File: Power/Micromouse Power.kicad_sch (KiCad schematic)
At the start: 24 parts, among them J1 Conn_02x08_Odd_Even, SW1 SW_SPST, U1 TP4056, U2 L9110S, U3 L9110S

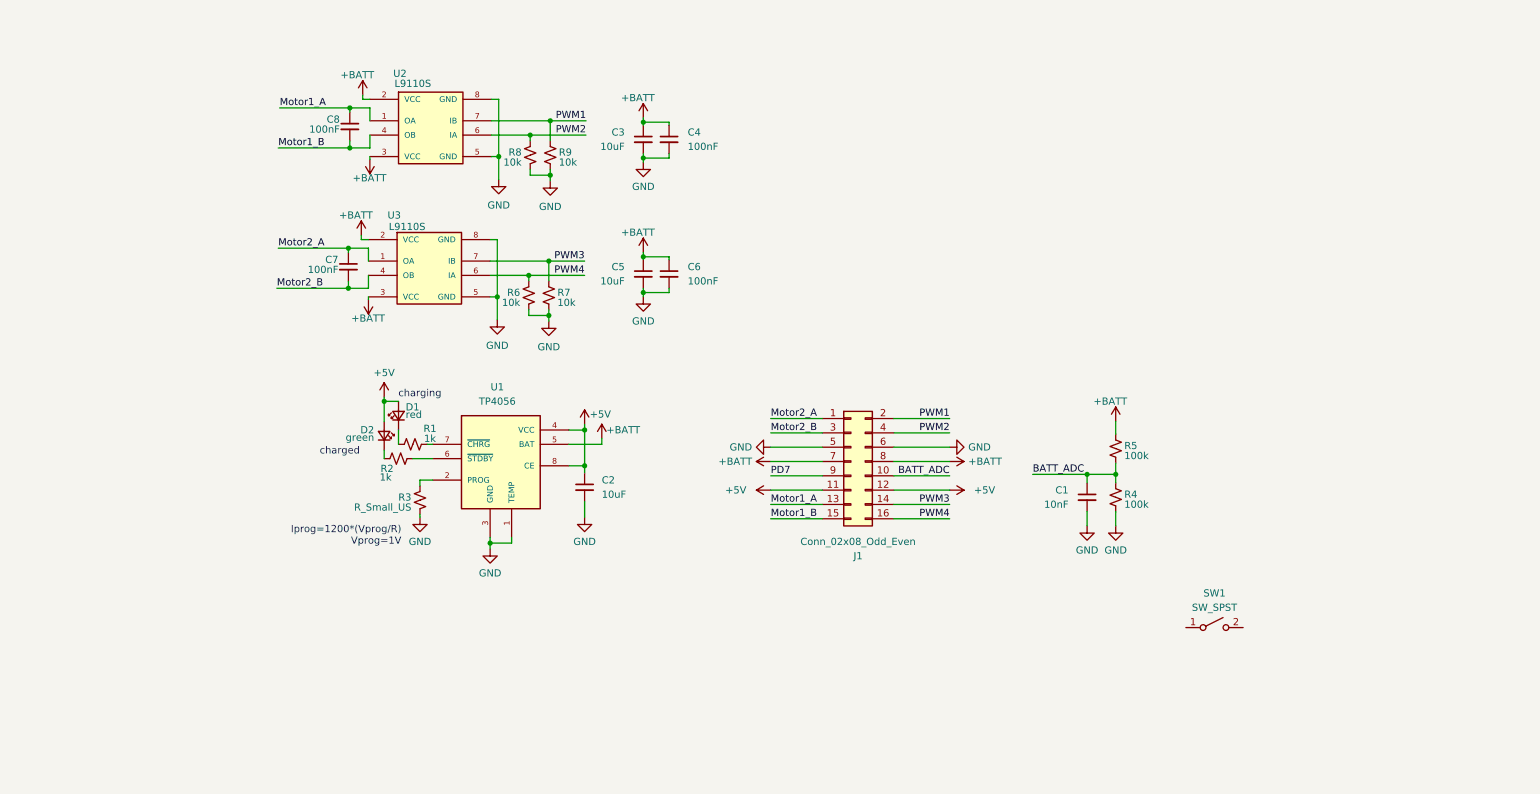
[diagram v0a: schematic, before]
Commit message: Added power flags
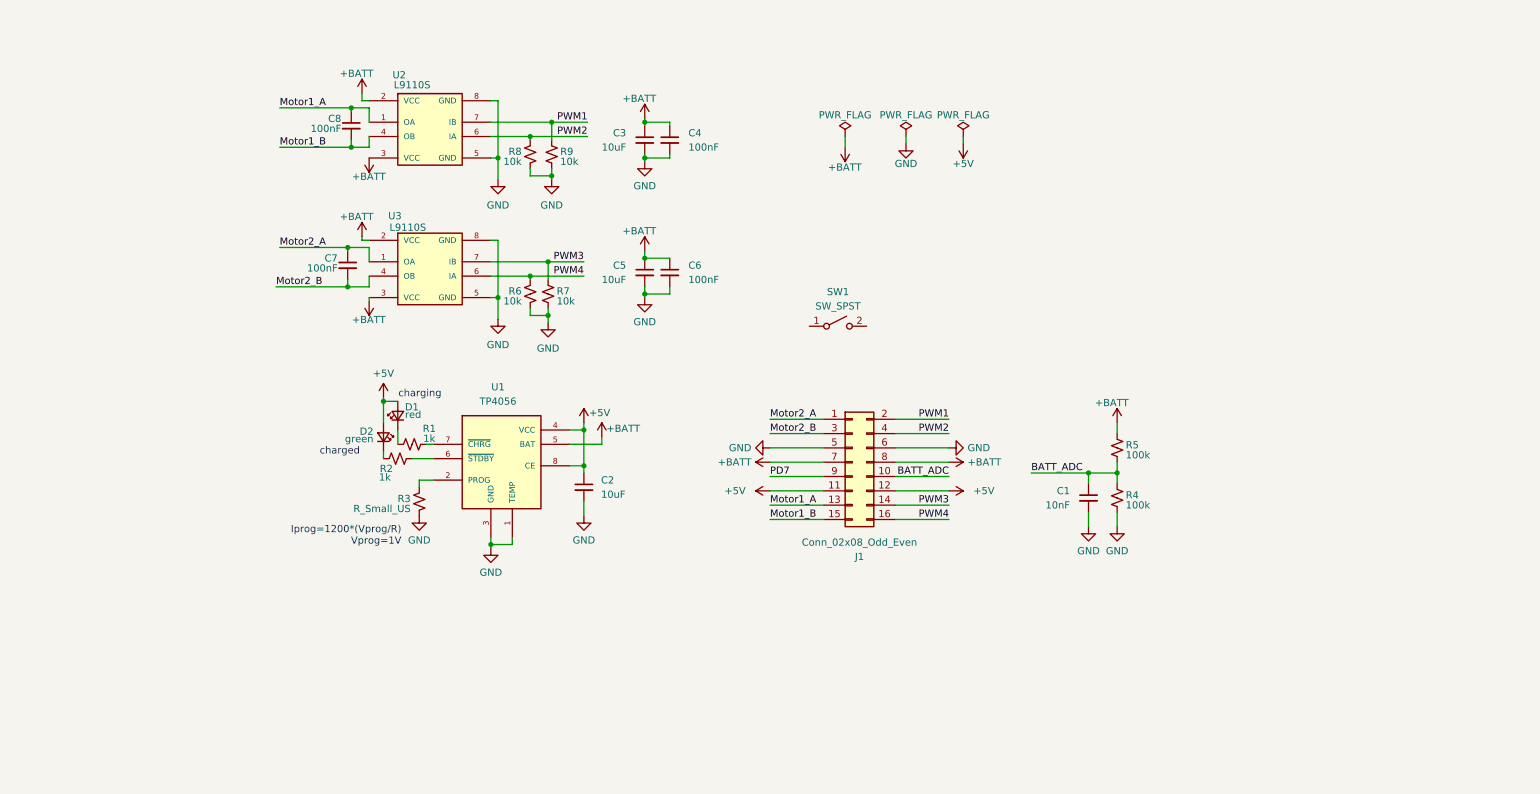
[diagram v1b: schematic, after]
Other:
- moved on the sheet: SW1

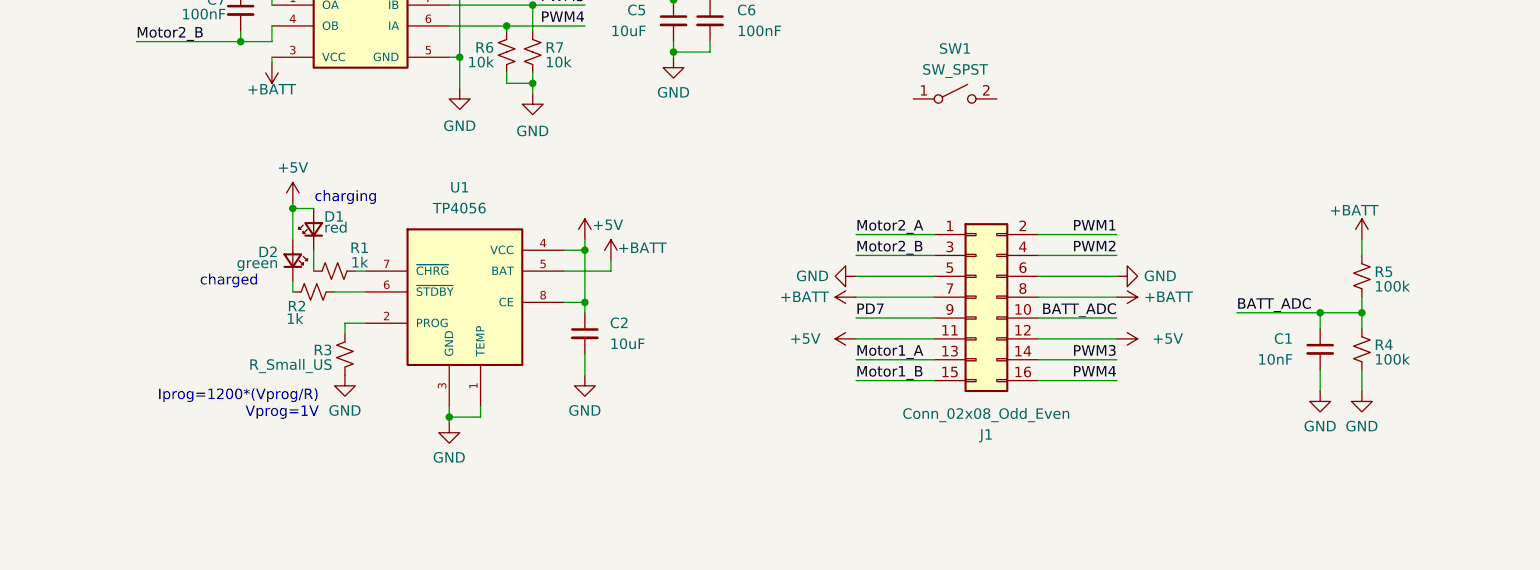
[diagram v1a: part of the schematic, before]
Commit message: Added test points and i_prog jumper.
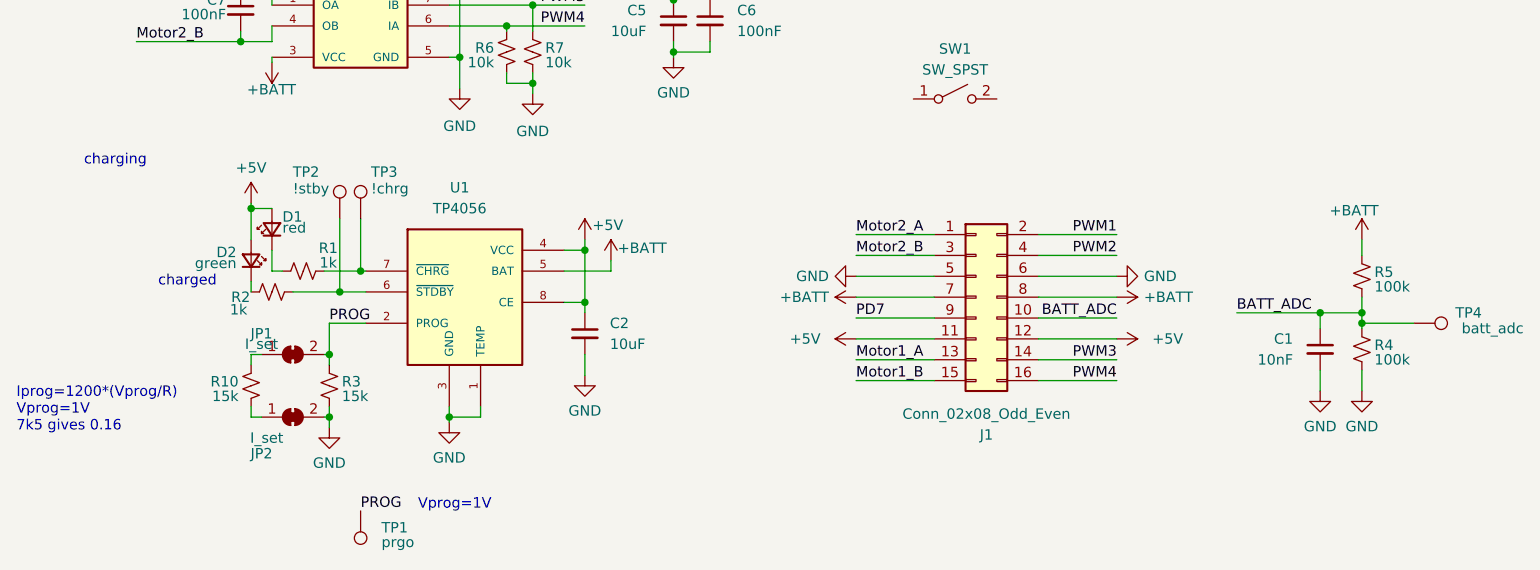
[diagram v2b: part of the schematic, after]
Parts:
- added JP1, JP2: I_set, TestPoint:TestPoint_2Pads_Pitch5.08mm_Drill1.3mm, symbol Jumper:SolderJumper_2_Bridged
- added R10: 15k, symbol Device:R_Small_US
- added TP1: prgo, symbol Connector:TestPoint
- added TP2: !stby, symbol Connector:TestPoint
- added TP3: !chrg, symbol Connector:TestPoint
- added TP4: batt_adc, symbol Connector:TestPoint
- R3: value R_Small_US -> 15k
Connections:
- net BATT_ADC: now also TP4.1
- net GND: now also JP2.2 (B)
- net at R1.2, U1.7 (~{CHRG}): now also TP3.1
- net PROG: now reaches R3.2, U1.2 (PROG)
- net PROG: now also JP1.2 (B), TP1.1
- net at R2.2, U1.6 (~{STDBY}): now also TP2.1
- new net: JP2.1 (A), R10.1
- new net: JP1.1 (A), R10.2
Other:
- note added: "Iprog=1200*(Vprog/R) Vprog=1V 7k5 gives 0.16"
- note added: "Vprog=1V"
- note removed: "Iprog=1200*(Vprog/R) Vprog=1V"
- moved on the sheet: D1, D2, R1, R2, R3

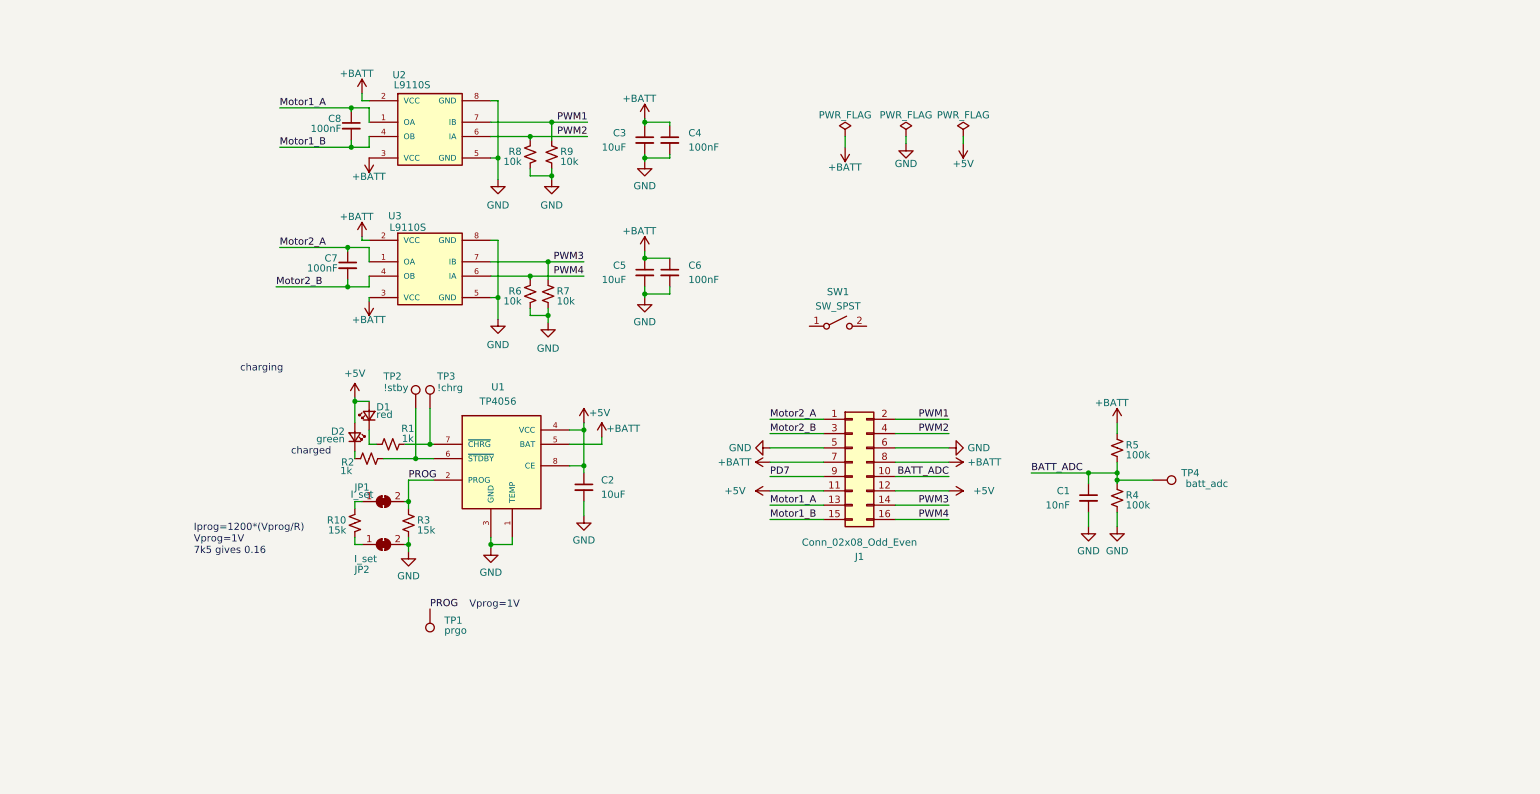
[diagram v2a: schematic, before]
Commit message: Added more test points and jumpers.
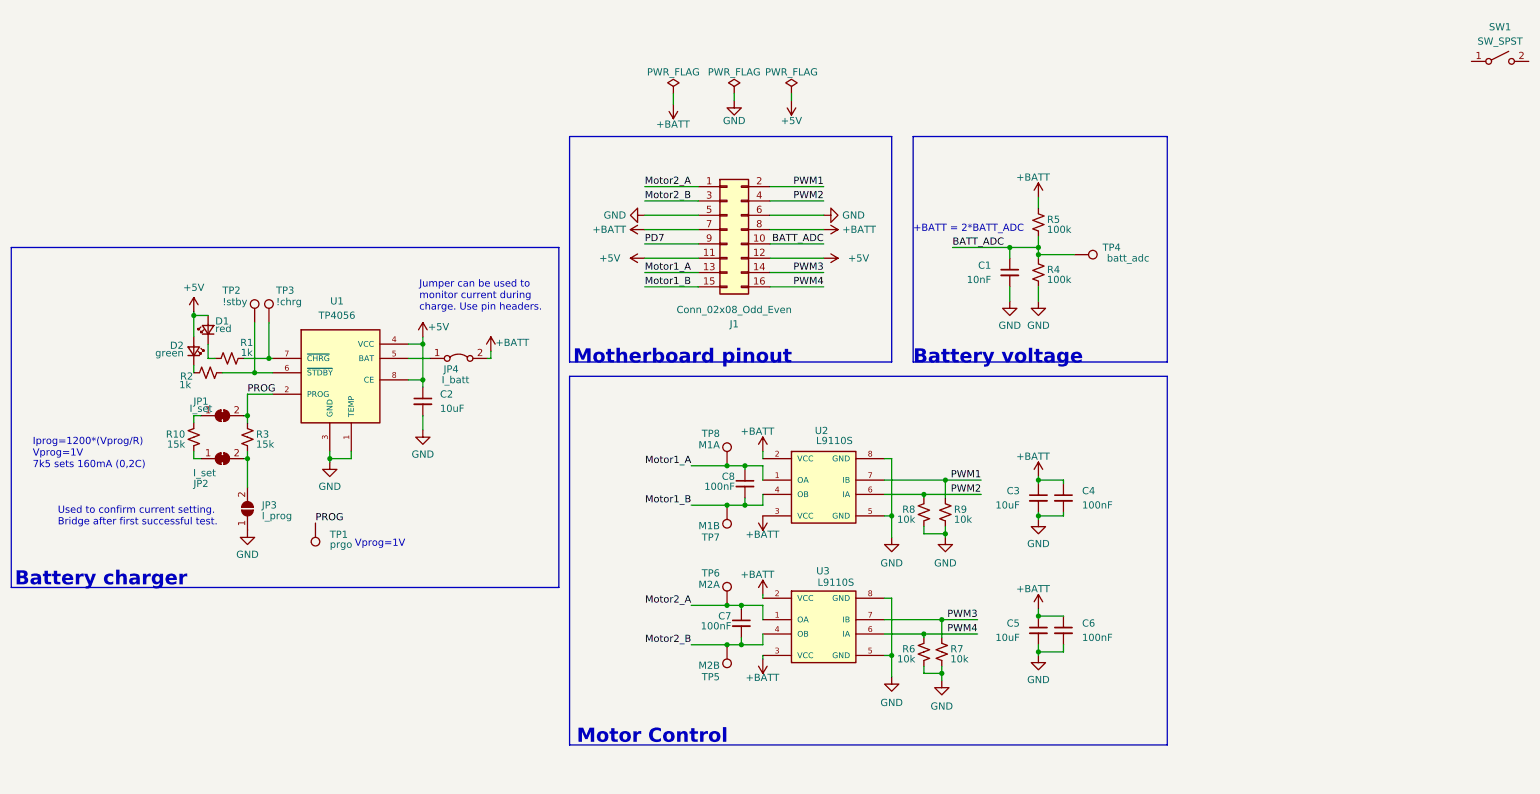
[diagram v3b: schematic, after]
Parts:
- added JP3: I_prog, Jumper:SolderJumper-2_P1.3mm_Open_RoundedPad1.0x1.5mm, symbol Jumper:SolderJumper_2_Open
- added JP4: I_batt, TestPoint:TestPoint_2Pads_Pitch2.54mm_Drill0.8mm, symbol Jumper:Jumper_2_Bridged
- added TP5: M2B, symbol Connector:TestPoint
- added TP6: M2A, symbol Connector:TestPoint
- added TP7: M1B, symbol Connector:TestPoint
- added TP8: M1A, symbol Connector:TestPoint
- J1: footprint (none) -> Connector_PinHeader_2.54mm:PinHeader_2x08_P2.54mm_Vertical
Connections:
- net +BATT: now also JP4.2 (B); no longer U1.5 (BAT)
- net GND: now also JP3.1 (A); no longer JP2.2 (B), R3.1
- net Motor1_A: now also TP8.1
- net Motor1_B: now also TP7.1
- net Motor2_A: now also TP6.1
- net Motor2_B: now also TP5.1
- new net: JP4.1 (A), U1.5 (BAT)
- new net: JP2.2 (B), JP3.2 (B), R3.1
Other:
- note added: "+BATT = 2*BATT_ADC"
- note added: "Battery charger"
- note added: "Battery voltage"
- note added: "Iprog=1200*(Vprog/R) Vprog=1V 7k5 sets 160mA (0,2C)"
- note added: "Jumper can be used to monitor current during charge. Use pin headers."
- note added: "Motherboard pinout"
- note added: "Motor Control"
- note added: "Used to confirm current setting. Bridge after first successful test."
- note removed: "Iprog=1200*(Vprog/R) Vprog=1V 7k5 gives 0.16"
- note removed: "charged"
- note removed: "charging"
- moved on the sheet: C1, C2, C3, C4, C5, C6, C7, C8, D1, D2, J1, JP1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

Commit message: Updated GPIO PC6-9 label on 08 connector
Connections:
- net PWM1 renamed PC6
- net PWM2 renamed PC7
- net PWM3 renamed PC8
- net PWM4 renamed PC9
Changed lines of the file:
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@@
     (effects (font (size 1.27 1.27)) (justify left bottom))
+  )
+  (label "PC6" (at 208.28 102.87 180) (fields_autoplaced)
+    (effects (font (size 1.27 1.27)) (justify right bottom))
   )
   (label "Motor2_A" (at 148.59 50.8 0) (fields_autoplaced)
@@
     (effects (font (size 1.27 1.27)) (justify right bottom))
   )
-  (label "PWM2" (at 208.28 105.41 180) (fields_autoplaced)
+  (label "PC8" (at 180.34 66.04 180) (fields_autoplaced)
     (effects (font (size 1.27 1.27)) (justify right bottom))
   )
-  (label "PWM3" (at 180.34 66.04 180) (fields_autoplaced)
-    (effects (font (size 1.27 1.27)) (justify right bottom))
-  )
-  (label "PWM4" (at 180.34 68.58 180) (fields_autoplaced)
+  (label "PC9" (at 180.34 68.58 180) (fields_autoplaced)
     (effects (font (size 1.27 1.27)) (justify right bottom))
   )
@@
     (effects (font (size 1.27 1.27)) (justify right bottom))
   )
-  (label "PWM1" (at 208.28 102.87 180) (fields_autoplaced)
-    (effects (font (size 1.27 1.27)) (justify right bottom))
-  )
   (label "PROG" (at 90.17 110.49 0) (fields_autoplaced)
     (effects (font (size 1.27 1.27)) (justify left bottom))
@@
     (effects (font (size 1.27 1.27)) (justify right bottom))
   )
+  (label "PC7" (at 208.28 105.41 180) (fields_autoplaced)
+    (effects (font (size 1.27 1.27)) (justify right bottom))
+  )
+  (label "PC8" (at 207.645 127.635 180) (fields_autoplaced)
+    (effects (font (size 1.27 1.27)) (justify right bottom))
+  )
   (label "Motor2_B" (at 148.59 53.34 0) (fields_autoplaced)
     (effects (font (size 1.27 1.27)) (justify left bottom))
   )
-  (label "PWM4" (at 207.645 130.175 180) (fields_autoplaced)
+  (label "PC9" (at 207.645 130.175 180) (fields_autoplaced)
     (effects (font (size 1.27 1.27)) (justify right bottom))
   )
-  (label "PWM1" (at 180.34 50.8 180) (fields_autoplaced)
+  (label "PC6" (at 180.34 50.8 180) (fields_autoplaced)
     (effects (font (size 1.27 1.27)) (justify right bottom))
   )
@@
     (effects (font (size 1.27 1.27)) (justify left bottom))
   )
-  (label "PWM3" (at 207.645 127.635 180) (fields_autoplaced)
+  (label "PC7" (at 180.34 53.34 180) (fields_autoplaced)
     (effects (font (size 1.27 1.27)) (justify right bottom))
   )
-  (label "PWM2" (at 180.34 53.34 180) (fields_autoplaced)
-    (effects (font (size 1.27 1.27)) (justify right bottom))
-  )

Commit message: Assigned some footprints
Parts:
- JP1, JP2: footprint TestPoint:TestPoint_2Pads_Pitch5.08mm_Drill1.3mm -> Jumper:SolderJumper-2_P1.3mm_Bridged_RoundedPad1.0x1.5mm
- JP4: footprint TestPoint:TestPoint_2Pads_Pitch2.54mm_Drill0.8mm -> Connector_PinHeader_2.54mm:PinHeader_1x02_P2.54mm_Vertical
- TP1, TP2, TP3, TP4, TP5, TP6, TP7, TP8: footprint (none) -> TestPoint:TestPoint_Pad_D1.0mm
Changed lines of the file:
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@@
       (effects (font (size 1.27 1.27)) (justify right))
     )
-    (property "Footprint" "" (at 224.79 67.945 0)
+    (property "Footprint" "TestPoint:TestPoint_Pad_D1.0mm" (at 224.79 67.945 0)
       (effects (font (size 1.27 1.27)) hide)
     )
@@
       (effects (font (size 1.27 1.27)) (justify left))
     )
-    (property "Footprint" "" (at 158.115 100.33 0)
+    (property "Footprint" "TestPoint:TestPoint_Pad_D1.0mm" (at 158.115 100.33 0)
       (effects (font (size 1.27 1.27)) hide)
     )
@@
       (effects (font (size 1.27 1.27)) (justify right))
     )
-    (property "Footprint" "" (at 85.09 110.49 0)
+    (property "Footprint" "TestPoint:TestPoint_Pad_D1.0mm" (at 85.09 110.49 0)
       (effects (font (size 1.27 1.27)) hide)
     )
@@
       (effects (font (size 1.27 1.27)) (justify right))
     )
-    (property "Footprint" "TestPoint:TestPoint_2Pads_Pitch2.54mm_Drill0.8mm" (at 115.57 81.28 0)
+    (property "Footprint" "Connector_PinHeader_2.54mm:PinHeader_1x02_P2.54mm_Vertical" (at 115.57 81.28 0)
       (effects (font (size 1.27 1.27)) hide)
     )
@@
       (effects (font (size 1.27 1.27)) (justify left))
     )
-    (property "Footprint" "" (at 86.995 74.93 0)
+    (property "Footprint" "TestPoint:TestPoint_Pad_D1.0mm" (at 86.995 74.93 0)
       (effects (font (size 1.27 1.27)) hide)
     )
@@
       (effects (font (size 1.27 1.27)) (justify left))
     )
-    (property "Footprint" "" (at 158.115 107.315 0)
+    (property "Footprint" "TestPoint:TestPoint_Pad_D1.0mm" (at 158.115 107.315 0)
       (effects (font (size 1.27 1.27)) hide)
     )
@@
       (effects (font (size 1.27 1.27)) (justify left))
     )
-    (property "Footprint" "" (at 84.455 74.93 0)
+    (property "Footprint" "TestPoint:TestPoint_Pad_D1.0mm" (at 84.455 74.93 0)
       (effects (font (size 1.27 1.27)) hide)
     )
@@
       (effects (font (size 1.27 1.27)) (justify left))
     )
-    (property "Footprint" "" (at 158.115 132.08 0)
+    (property "Footprint" "TestPoint:TestPoint_Pad_D1.0mm" (at 158.115 132.08 0)
       (effects (font (size 1.27 1.27)) hide)
     )
@@
       (effects (font (size 1.27 1.27)) (justify left))
     )
-    (property "Footprint" "" (at 158.115 125.095 0)
+    (property "Footprint" "TestPoint:TestPoint_Pad_D1.0mm" (at 158.115 125.095 0)
       (effects (font (size 1.27 1.27)) hide)
     )
@@
       (effects (font (size 1.27 1.27)))
     )
-    (property "Footprint" "TestPoint:TestPoint_2Pads_Pitch5.08mm_Drill1.3mm" (at 73.66 91.44 0)
+    (property "Footprint" "Jumper:SolderJumper-2_P1.3mm_Bridged_RoundedPad1.0x1.5mm" (at 73.66 91.44 0)
       (effects (font (size 1.27 1.27)) hide)
     )
@@
       (effects (font (size 1.27 1.27)))
     )
-    (property "Footprint" "TestPoint:TestPoint_2Pads_Pitch5.08mm_Drill1.3mm" (at 73.66 99.06 0)
-      (effects (font (size 1.27 1.27)) hide)
-    )
+    (property "Footprint" "Jumper:SolderJumper-2_P1.3mm_Bridged_RoundedPad1.0x1.5mm" (at 73.66 99.06 0)
+      (effects (font (size 1.27 1.27)) hide)
+    )
